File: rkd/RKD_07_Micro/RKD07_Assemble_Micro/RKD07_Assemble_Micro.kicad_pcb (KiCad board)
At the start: 2 copper layers, 98.8 x 85.7 mm, 169 parts, among them J1 Conn_01x06, J2 Conn_01x06, J3 Conn_01x04, J4 Conn_01x02, J5 Conn_01x06, J53 Qwiic_RA, J6 Conn_01x02, J9 Conn_01x06, SW1 SW_Push, SW10 SW_Push, SW11 SW_Push, SW12 SW_Push, SW13 SW_Push, SW14 SW_Push, SW15 SW_Push, SW16 SW_Push, SW17 SW_Push, SW18 SW_Push, SW19 SW_Push, SW2 SW_Push, SW20 SW_Push, SW21 SW_Push, SW22 SW_Push, SW23 SW_Push, SW24 SW_Push, SW25 SW_Push, SW26 SW_Push, SW27 SW_Push, SW28 SW_Push, SW29 SW_Push, SW3 SW_Push, SW30 SW_Push, SW31 SW_Push, SW4 SW_Push, SW49 RotaryEncoder_Switch, SW5 SW_Push, SW51 SW_Push, SW52 SW_Push, SW53 SW_Push, SW54 SW_Push, SW55 SW_Push, SW56 SW_Push, SW57 SW_Push, SW58 SW_Push, SW59 SW_Push, SW6 SW_Push, SW60 SW_Push, SW61 SW_Push, SW62 SW_Push, SW63 SW_Push, SW64 SW_Push, SW65 SW_Push, SW66 SW_Push, SW67 SW_Push, SW68 SW_Push, SW69 SW_Push, SW7 SW_Push, SW70 SW_Push, SW71 SW_Push, SW72 SW_Push, SW73 SW_Push, SW74 SW_Push, SW75 SW_Push, SW76 SW_Push, SW77 SW_Push, SW78 SW_Push, SW79 SW_Push, SW8 SW_Push, SW80 SW_Push, SW81 SW_Push, SW82 SW_Push, SW83 SW_Push, SW84 SW_Push, SW85 SW_Push, SW86 SW_Push, SW87 SW_Push, SW88 SW_Push, SW89 SW_Push, SW9 SW_Push, SW90 SW_Push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

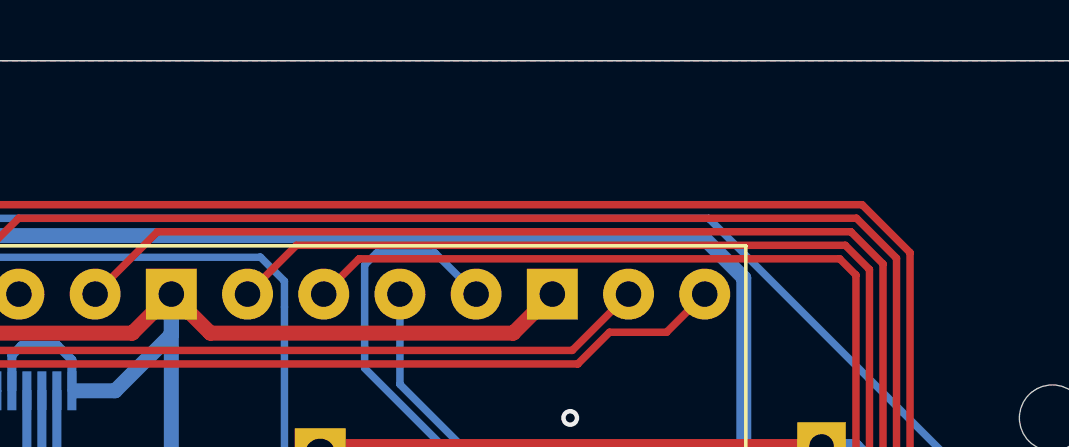
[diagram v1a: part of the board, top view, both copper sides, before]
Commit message: miniシリーズのネジ穴追加
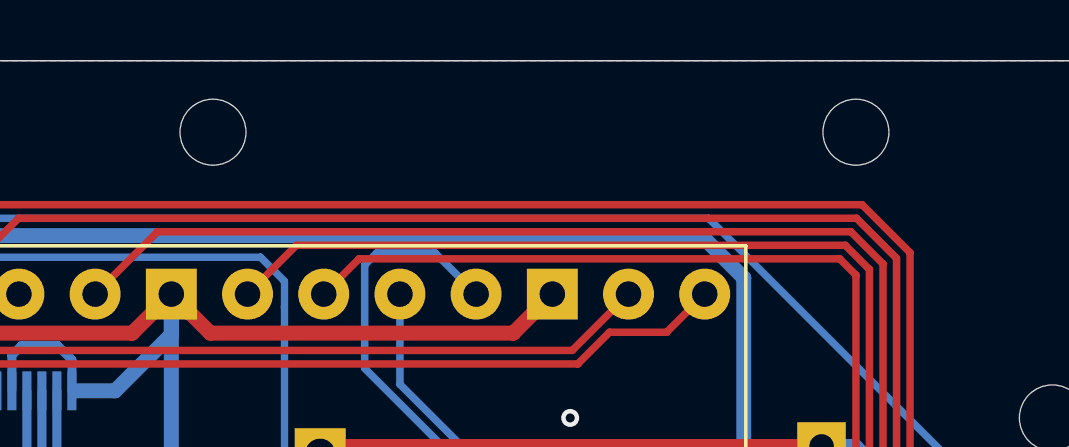
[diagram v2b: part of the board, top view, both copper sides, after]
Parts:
- added Ref**: Val**, kbd_Hole:m2_Screw_Hole, F.Cu at (57.1, 21.4)
- added Ref**: Val**, kbd_Hole:m2_Screw_Hole, F.Cu at (78.6, 21.4)
